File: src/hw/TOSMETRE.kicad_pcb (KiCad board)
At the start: 2 copper layers, 4.5 x 3.5 mm, 61 parts, among them J1 Barrel_Jack_Switch, J2 Conn_01x02_Male, J3 Conn_01x08_Male, J4 Conn_Coaxial, J5 Conn_01x05_Male, J6 Conn_01x02_Male, J7 Conn_Coaxial, SW1 SW_DIP_x01, U1 TPS70950DBVT, U2 18F1320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

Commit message: #305
LIVRAISON SUITE A TELEPHONE 2 ET AVANT DE POURSUIVRE SI PAS BON
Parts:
- moved D3 18.7 mm to (236.9, 50.2), turned to 90 degrees
- moved C19 14.9 mm to (263.7, 40.5)
- moved J4 14.7 mm to (271.0, 42.0), turned to 180 degrees
- moved C5 14.1 mm to (246.3, 40.4)
- moved L1 13.5 mm to (258.8, 42.0)
- moved C13 13.3 mm to (214.0, 41.9)
- moved C14 13.3 mm to (214.0, 36.6)
- moved D2 13.3 mm to (250.1, 41.9)
- moved R21 13.3 mm to (210.2, 48.5)
- moved R4 13.3 mm to (241.7, 41.9)
- moved R19 13.3 mm to (205.1, 48.5)
- moved R6 13.3 mm to (236.9, 45.9)
- moved R7 13.3 mm to (236.9, 38.1)
- moved R8 13.3 mm to (232.9, 41.9)
- moved U3 13.3 mm to (219.1, 45.7)
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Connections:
- C13 pad 2: Net-(C13-Pad2) -> Net-(C10-Pad2)
- C14 pad 2: Net-(C13-Pad2) -> Net-(C10-Pad2)
- R7 pad 2: Net-(C13-Pad2) -> Net-(C10-Pad2)
- U3 pad 5: Net-(C13-Pad2) -> Net-(C10-Pad2)
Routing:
- net Net-(C10-Pad2): track 246.0 -> 347.0 mm
- net Net-(C13-Pad2): track 31.9 -> 0.00 mm
- net Net-(D3-Pad2): track 9.08 -> 2.16 mm
- net Net-(C15-Pad2): track 26.3 -> 19.5 mm
- net Net-(C21-Pad1): track 9.20 -> 5.27 mm
- net Net-(C18-Pad2): track 17.5 -> 13.7 mm
- net Net-(C12-Pad1): track 10.6 -> 6.98 mm
- net Net-(C20-Pad1): track 10.1 -> 6.60 mm
- net Net-(C22-Pad1): track 6.14 -> 9.12 mm
- net Net-(R8-Pad1): track 16.4 -> 13.8 mm
- net Net-(D5-Pad2): track 4.25 -> 1.90 mm
- net Net-(C5-Pad1): track 8.55 -> 6.22 mm
- net Net-(C19-Pad1): track 5.76 -> 8.04 mm
- net GNDREF: track 151.5 -> 153.4 mm
- net Net-(R16-Pad1): track 30.7 -> 32.3 mm

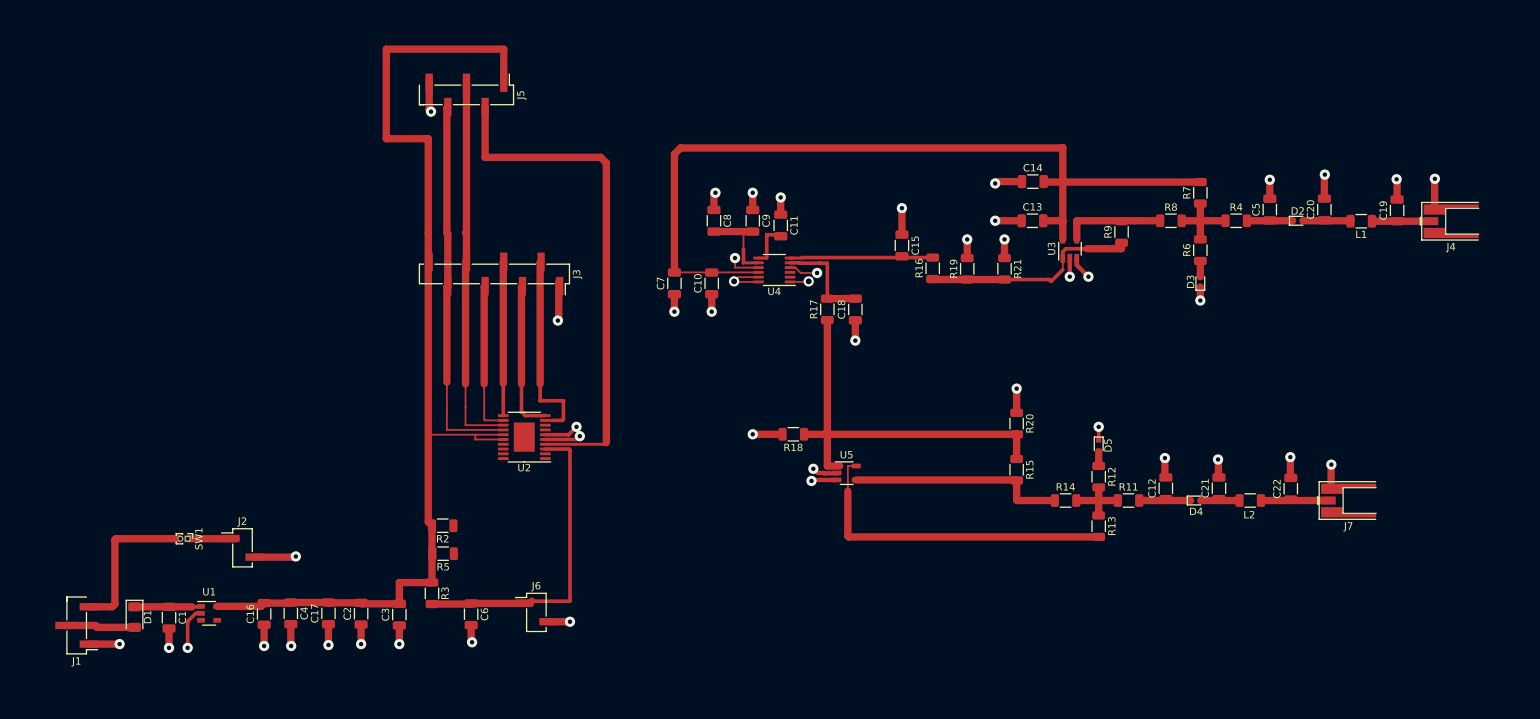
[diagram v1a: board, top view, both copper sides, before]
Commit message: #305
MODIFICATION CIRCUIT
RAPPROCHEMENT DES COMPOSANTS SUR PISTES
RAJOUT PLAN DE MASSE
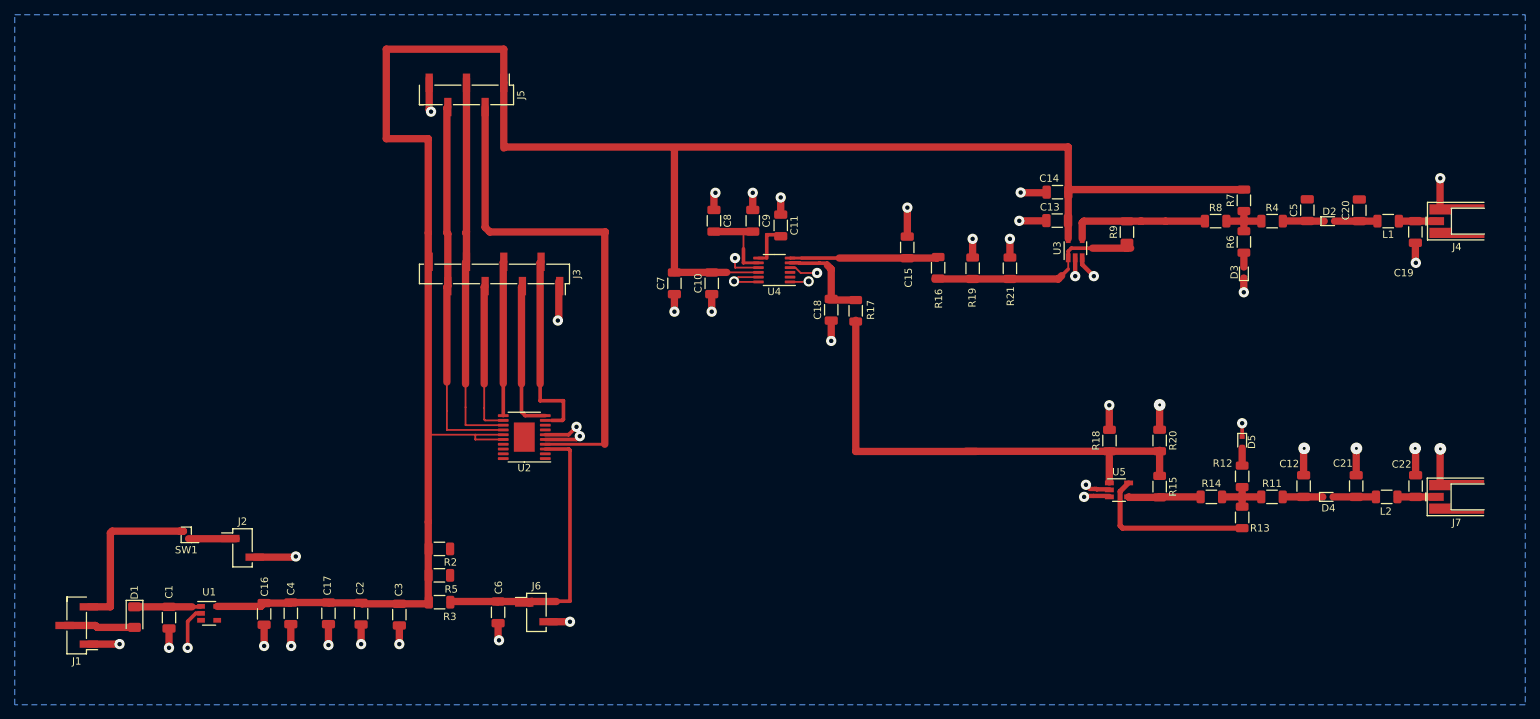
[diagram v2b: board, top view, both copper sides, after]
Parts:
- SW1: footprint Connector_PinHeader_1.00mm:PinHeader_1x02_P1.00mm_Vertical -> Connector_PinHeader_1.00mm:PinHeader_1x02_P1.00mm_Vertical_SMD_Pin1Left
- moved R18 43.1 mm to (224.5, 71.8), turned to 90 degrees
- moved U5 37.2 mm to (225.8, 78.6)
- moved R14 19.9 mm to (238.4, 79.5)
- moved R15 19.6 mm to (231.3, 78.1)
- moved R20 19.6 mm to (231.3, 71.8)
- moved R13 19.6 mm to (242.5, 82.3)
- moved D5 19.5 mm to (242.5, 72.0)
- moved R11 19.5 mm to (246.6, 79.5)
- moved R12 19.5 mm to (242.5, 76.7)
- moved C12 18.8 mm to (250.9, 78.0)
- moved C21 18.7 mm to (258.1, 78.0)
- moved L2 18.6 mm to (262.2, 79.5)
- moved D4 18.0 mm to (254.2, 79.5)
- moved C22 17.0 mm to (266.2, 78.0)
- moved J7 14.7 mm to (271.8, 79.5)
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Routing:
- net Net-(R14-Pad1): track 29.7 -> 9.55 mm
- net Net-(C10-Pad2): track 347.0 -> 364.5 mm
- net Net-(R15-Pad1): track 54.0 -> 67.6 mm
- net Net-(C15-Pad2): track 19.5 -> 32.9 mm
- net Net-(R8-Pad1): track 13.8 -> 19.1 mm
- net Net-(C22-Pad1): track 9.12 -> 5.31 mm
- net Net-(R4-Pad1): track 11.1 -> 7.51 mm
- net Net-(C19-Pad1): track 8.04 -> 5.15 mm
- net Net-(J1-Pad3): track 21.3 -> 23.1 mm
- net GNDREF: track 153.4 -> 151.7 mm, vias 46 -> 44
- net Net-(R11-Pad1): track 9.56 -> 8.00 mm
- net Net-(C12-Pad1): track 6.98 -> 5.46 mm
- net Net-(C6-Pad1): track 43.0 -> 44.2 mm
- net Net-(C20-Pad1): track 6.60 -> 5.84 mm
- net Net-(C21-Pad1): track 5.27 -> 5.84 mm
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- added copper zone on B.Cu, net GNDREF

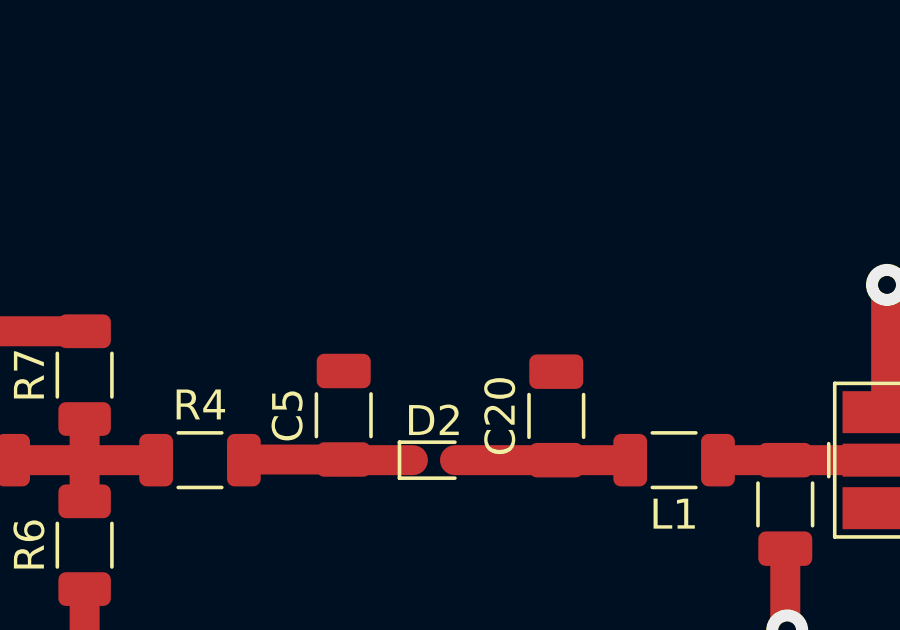
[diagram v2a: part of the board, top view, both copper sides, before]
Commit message: #305
Ajout de masse oublier sur C5 et C20
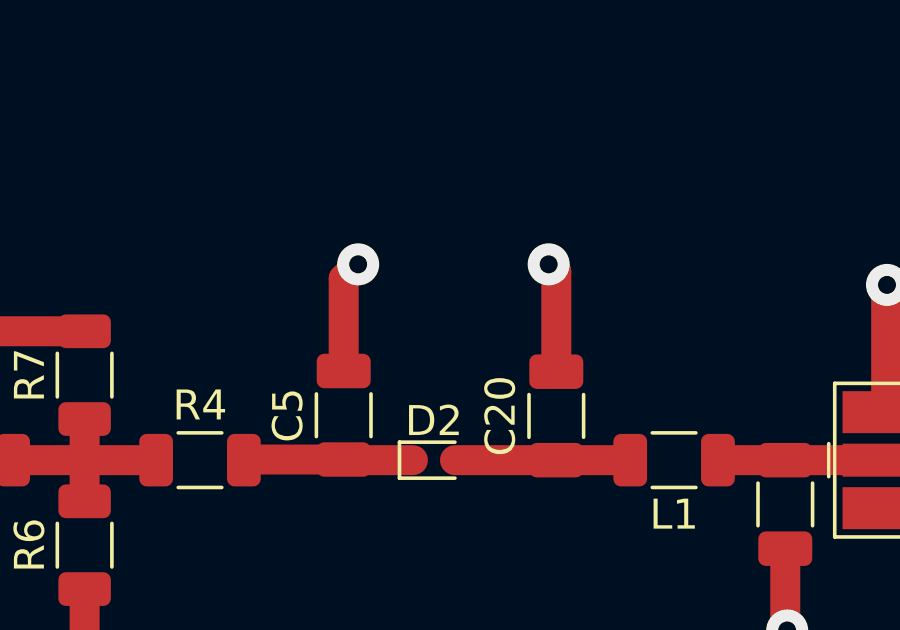
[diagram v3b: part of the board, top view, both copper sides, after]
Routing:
- net GNDREF: track 151.7 -> 159.1 mm, vias 44 -> 46

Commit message: #173
Mise a jour suite a la version kicad 6
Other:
- net class Default removed

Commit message: #402
BROULLION
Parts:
- moved R5 28.0 mm to (160.5, 83.9), turned to -90 degrees
- moved R3 21.9 mm to (146.7, 76.6)
- moved J6 18.4 mm to (153.0, 78.1)
- moved C6 16.7 mm to (152.5, 82.9), turned to 0 degrees
- moved R2 13.9 mm to (146.5, 82.6), turned to -90 degrees
- moved J3 0.25 mm to (140.7, 49.4)
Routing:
- net Net-(C6-Pad1): track 44.2 -> 3.42 mm

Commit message: #406
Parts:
- U4: footprint Package_SO:MSOP-12_3x4mm_P0.65mm -> Package_SO:MSOP-8_3x3mm_P0.65mm
- moved C16 157.5 mm to (257.0, 40.5), turned to 0 degrees
- moved C17 153.9 mm to (261.9, 40.5), turned to 0 degrees
- moved J7 105.5 mm to (166.4, 84.5), turned to 0 degrees
- moved J3 100.0 mm to (41.1, 40.5), turned to 0 degrees
- moved J4 97.8 mm to (176.9, 65.7), turned to 0 degrees
- moved D2 92.4 mm to (189.7, 107.8)
- moved SW1 90.9 mm to (189.3, 93.2), turned to 0 degrees
- moved L2 84.8 mm to (179.0, 96.2)
- moved C18 81.5 mm to (266.9, 40.5), turned to 0 degrees
- moved C2 80.0 mm to (180.8, 40.5), turned to -90 degrees
- moved C3 79.9 mm to (185.9, 40.7), turned to -90 degrees
- moved D3 76.0 mm to (194.8, 107.8), turned to 0 degrees
- moved R17 74.7 mm to (261.9, 34.2), turned to 0 degrees
- moved R21 73.9 mm to (283.5, 34.2), turned to 0 degrees
- moved R19 67.9 mm to (272.2, 34.2), turned to 0 degrees
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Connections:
- U1 pad 3: Net-(U1-Pad3) -> unconnected-(U1-Pad3)
- U1 pad 4: Net-(U1-Pad4) -> unconnected-(U1-Pad4)
- U2 pad 1: Net-(U2-Pad1) -> unconnected-(U2-Pad1)
- U2 pad 17: Net-(U2-Pad17) -> unconnected-(U2-Pad17)
- U2 pad 18: Net-(U2-Pad18) -> unconnected-(U2-Pad18)
- U2 pad 19: Net-(U2-Pad19) -> unconnected-(U2-Pad19)
- U2 pad 2: Net-(U2-Pad2) -> unconnected-(U2-Pad2)
- U2 pad 20: Net-(U2-Pad20) -> unconnected-(U2-Pad20)
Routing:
- net Net-(C10-Pad2): track 364.5 -> 0.00 mm
- net GNDREF: track 159.1 -> 0.00 mm, vias 46 -> 0
- net Net-(J3-Pad6): track 73.2 -> 0.00 mm
- net Net-(J3-Pad7): track 72.1 -> 0.00 mm
- net Net-(J5-Pad2): track 70.1 -> 0.00 mm
- net Net-(R15-Pad1): track 67.6 -> 0.00 mm
- net Net-(C15-Pad2): track 32.9 -> 0.00 mm
- net Net-(R16-Pad1): track 31.9 -> 0.00 mm
- net Net-(J3-Pad2): track 26.4 -> 0.00 mm
- net Net-(J1-Pad3): track 23.1 -> 0.00 mm
- net Net-(J3-Pad4): track 21.0 -> 0.00 mm
- net Net-(J3-Pad5): track 20.9 -> 0.00 mm
- net Net-(J3-Pad3): track 20.6 -> 0.00 mm
- net Net-(R8-Pad1): track 19.1 -> 0.00 mm
- net Net-(C18-Pad2): track 14.0 -> 0.00 mm
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- removed copper zone on B.Cu, net GNDREF

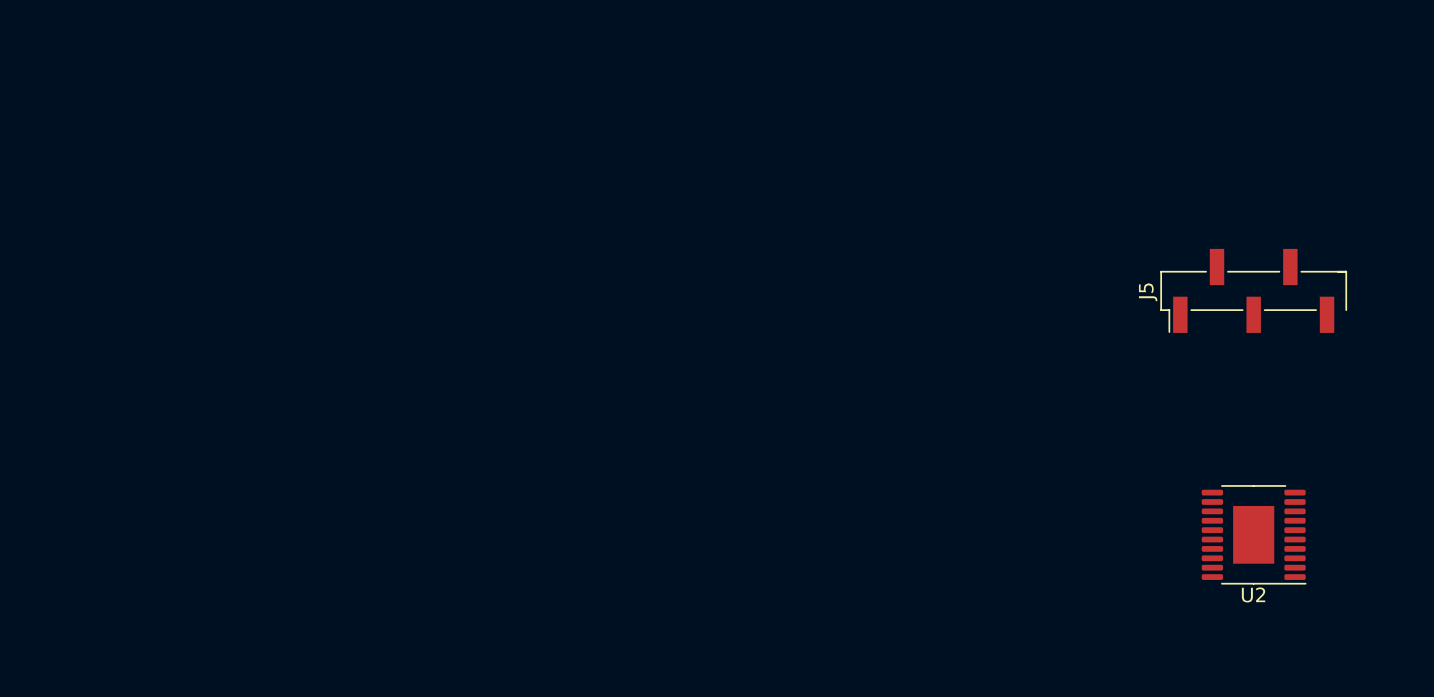
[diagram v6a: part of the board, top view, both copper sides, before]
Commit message: #406
pour verification 18F1320 sans pave
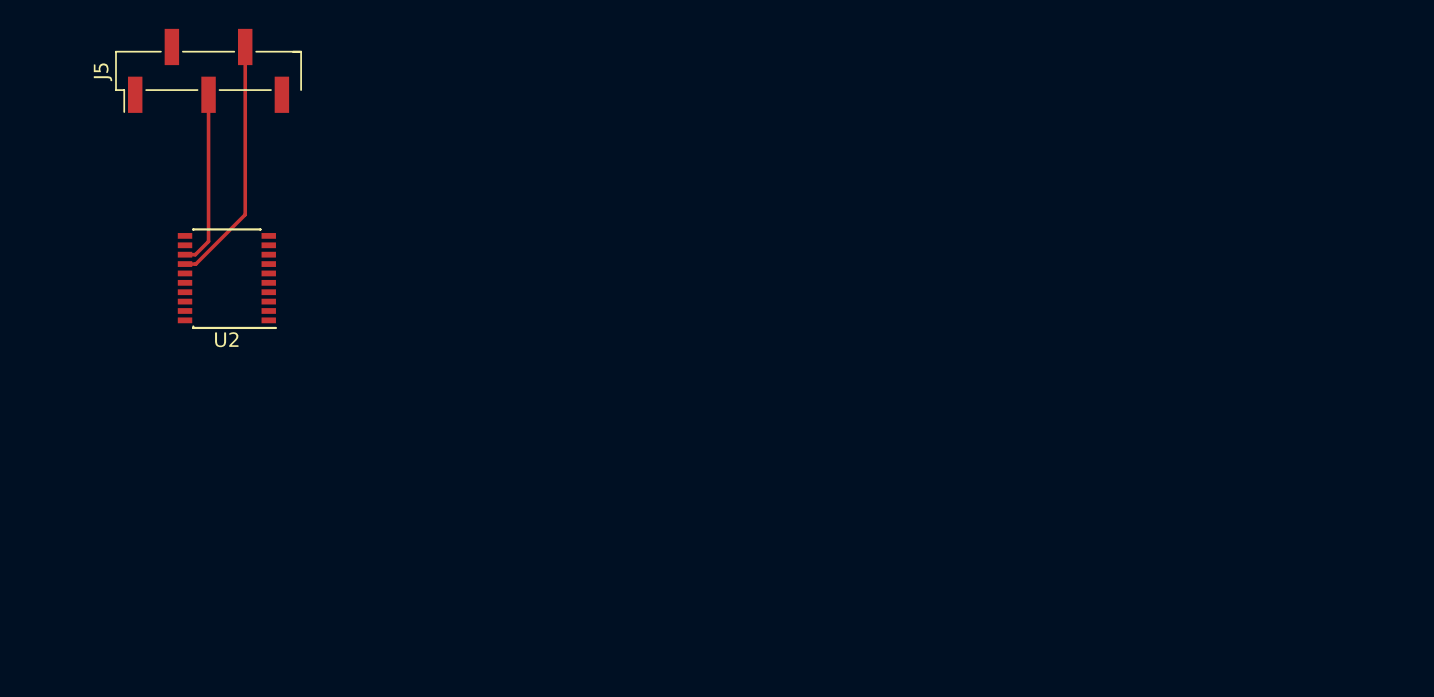
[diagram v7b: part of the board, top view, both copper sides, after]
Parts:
- U2: footprint Package_SO:HTSSOP-20-1EP_4.4x6.5mm_P0.65mm_EP2.85x4mm -> Package_SO:SSOP-20_4.4x6.5mm_P0.65mm
- moved J5 74.0 mm to (76.6, 24.9)
- moved U2 73.3 mm to (77.9, 39.2)
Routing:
- net Net-(J3-Pad7): track 0.00 -> 17.2 mm
- net Net-(J3-Pad6): track 0.00 -> 12.2 mm

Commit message: #406
DEBUT DU ROUTAGE
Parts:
- moved C2 114.3 mm to (66.6, 46.2), turned to 90 degrees
- moved C3 114.1 mm to (71.9, 46.3), turned to 90 degrees
- moved C6 113.4 mm to (89.1, 44.6), turned to -90 degrees
- moved R3 108.0 mm to (78.9, 48.0)
- moved J6 88.4 mm to (99.0, 44.6)
- moved J5 0.65 mm to (76.0, 25.0)
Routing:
- net Net-(C10-Pad2): track 0.00 -> 125.7 mm
- net Net-(J3-Pad2): track 0.00 -> 104.6 mm
- net Net-(J3-Pad3): track 0.00 -> 96.2 mm
- net Net-(J5-Pad2): track 0.00 -> 80.6 mm
- net Net-(J3-Pad6): track 12.2 -> 50.3 mm
- net GNDREF: track 0.00 -> 37.7 mm, vias 0 -> 7
- net Net-(J3-Pad4): track 0.00 -> 36.8 mm
- net Net-(J3-Pad7): track 17.2 -> 53.2 mm
- net Net-(J3-Pad5): track 0.00 -> 34.3 mm
- net Net-(C6-Pad1): track 0.00 -> 29.7 mm
